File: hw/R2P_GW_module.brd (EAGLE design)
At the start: 40 x 40 mm, 32 parts, among them U1 STM32F103CX, U5 LD3985XX, X1 MICROMATCH-4

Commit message: First PCB version almost finished
Andrea Zoppi
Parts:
- removed U$1: ASE, crystal:ASE
- added C10, C13, C14, C15, C16, C17, C22, C23, C25, C26, C27, C8: 100n, rcl:C0603
- added C12: 4u7, rcl:C0805
- added C2, C3: 2u2, rcl:C0805
- added C24: 10u, rcl:C0805
- added C28: 15p, rcl:C0603
- added C4: 1u, rcl:C0805
- added OSC1: ASE 8MHz, crystal:ASE
- added OSC2: ASE 50MHz, crystal:ASE
- added R10, R15, R7: 2k2, rcl:R0603
- added R11, R14: 22, rcl:R0603
- added R12: 100k, rcl:R0603
- added R13: 1k5, rcl:R0603
- added R5: 47, rcl:R0603
- added R6: 4k87, rcl:R0603
- added R8, R9: 220, rcl:R0603
- added RN1, RN3, RN5: 51, resistor-dil:CAT16
- added RN2, RN4: 2k2, resistor-dil:CAT16
- added U2: DP83848C, texas-instruments:LQFP48
- added X2: 47589-0001, molex:47589-0001
- added X3: (no value), bel:SI-60062-F
- C11: value 15pF -> 15p
- C21: value 4.7u -> 4u7
- R2: value 10k -> 100k
- U1: value STM32F103CX -> STM32F407VG; device st:LQFP48 -> st:LQFP100
- moved C21 27.5 mm to (2.97, 25.5), turned to 90 degrees
- moved C20 24.2 mm to (8.54, 17.6), turned to 90 degrees
- moved C1 18.1 mm to (8.00, 38.0), turned to 90 degrees
- moved C11 16.7 mm to (28.0, 20.0), turned to 0 degrees
- moved R2 12.4 mm to (21.9, 15.5), turned to 270 degrees
- moved R3 10.0 mm to (28.0, 26.5), turned to 180 degrees
- moved U1 8.57 mm to (17.0, 26.0), turned to 180 degrees
- moved C19 6.40 mm to (24.1, 15.5)
- moved C18 1.19 mm to (28.0, 18.1), turned to 0 degrees
- moved X1 0.50 mm to (34.8, 35.2)
- renumbered SOT1 to U4, U5 to U3
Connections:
- removed net AM_DRDY: U1.41
- removed net AM_INT1: U1.42
- removed net AM_INT2: U1.43
- removed net BOOT0: R2.2, U1.44
- removed net GPS_RESET: U1.14
- removed net GPS_RX: U1.13
- removed net GPS_STATUS: U1.11
- removed net GPS_TX: U1.12
- removed net GYRO_CS: U1.18
- removed net GYRO_INT1: U1.21
- removed net GYRO_INT2: U1.19
- removed net MISO: U1.16
- removed net MOSI: U1.17
- removed net NRST: U$4.P$10, U1.7
- removed net OSC_IN: U$1.3, U1.5
- removed net OSC_OUT: U1.6
- removed net SCK: U1.15
- removed net SCL: U1.45
- removed net SDA: U1.46
- new net !ETH_PWRDN: OSC2.1, RN4.6, U2.7
- new net !RESET: R15.1, RN2.1, U$4.10, U1.14, U2.29
- new net ETH_RMII_CRS_DV: RN5.2, U1.32
- new net ETH_RMII_MDC: U1.16, U2.31
- new net ETH_RMII_MDIO: R13.1, U1.25, U2.30
- new net ETH_RMII_REF_CLK: OSC2.3, U1.24, U2.34
- new net ETH_RMII_RXD0: RN5.3, U1.33
- new net ETH_RMII_RXD1: RN5.4, U1.34
- new net ETH_RMII_TXD0: RN3.3, U1.51
- new net ETH_RMII_TXD1: RN3.4, U1.52
- new net ETH_RMII_TXEN: RN3.2, U1.48
- new net MCU_CLK: OSC1.3, U1.12
- new net N$10: RN1.3, U2.14, X3.4
- new net N$11: RN1.4, U2.13, X3.6
- new net N$12: R9.2, X3.YA
- new net N$13: C14.2, X3.2
- new net N$14: C17.1, C22.1, C23.1, C24.1, U2.18, U2.23, U2.37
- new net N$16: C16.2, X3.5
- new net N$17: R8.2, X3.GA
- new net N$19: RN2.3, U2.27
- new net N$21: RN3.7, U2.2
- new net N$23: RN2.2, U2.28, X3.YK
- new net N$24: RN2.4, U2.26, X3.GK
- new net N$25: RN3.6, U2.3
- new net N$26: R2.1, U1.94
- new net N$27: R7.1, U2.20
- new net N$28: R10.1, U2.21
- new net N$29: RN3.5, U2.4
- new net N$30: RN4.8, U2.5
- new net N$31: RN4.7, U2.6
- new net N$32: R14.2, X2.3
- new net N$34: RN5.6, U2.43
- new net N$38: R12.1, U2.39
- new net N$40: RN5.5, U2.44
- new net N$41: RN5.7, U2.40
- new net N$6: R6.1, U2.24
- new net N$7: R11.2, X2.2
- new net N$8: RN1.1, U2.17, X3.1
- new net N$9: RN1.2, U2.16, X3.3
- new net USB_DM: R11.1, U1.70
- new net USB_DP: R14.1, U1.71
- new net USB_ID: U1.69, X2.4
- new net USB_VBUS: U1.68, X2.1
- new net VCAP_1: C3.1, U1.49
- new net VCAP_2: C2.1, U1.73
- net +3V3: now also C10.1, C12.1, C13.1, C15.1, C25.1, C26.1, C27.1, C28.1, OSC1.4, OSC2.4, R10.2, R12.2, R13.2, R15.2, R5.2, R7.2, R8.1, R9.1, RN1.5, RN1.6, RN1.7, RN1.8, RN2.5, RN2.6, RN2.7, RN2.8, RN4.3, U$4.1, U1.100, U1.11, U1.19, U1.22, U1.28, U1.50, U1.6, U1.75, U2.22, U2.32, U2.48; no longer U$1.4, U$4.P$1, U1.1, U1.24, U1.36, U1.48, U1.9
- net CAN_RX: now also U1.81; no longer U1.32
- net CAN_TX: now also U1.82; no longer U1.33
- net GND: now also C10.2, C12.2, C13.2, C14.1, C15.2, C16.1, C17.2, C2.2, C22.2, C23.2, C24.2, C25.2, C26.2, C27.2, C28.2, C3.2, C4.2, C8.2, OSC1.2, OSC2.2, R2.2, R6.2, RN3.1, RN3.8, RN4.1, RN4.2, RN4.4, RN4.5, RN5.1, RN5.8, U$4.3, U$4.5, U$4.9, U1.10, U1.20, U1.27, U1.74, U1.99, U2.15, U2.19, U2.35, U2.36, U2.47, X2.5, X2.SHLD1, X2.SHLD2, X2.SHLD3, X2.SHLD4, X3.8, X3.SHLD1, X3.SHLD2; no longer R2.1, U$1.2, U$4.P$3, U$4.P$9, U1.23, U1.35, U1.47, U1.8
- net JTCK: now also U$4.4, U1.76; no longer U$4.P$4, U1.37
- net JTDI: now also U$4.8, U1.77; no longer U$4.P$8, U1.38
- net JTDO: now also U$4.6, U1.89; no longer U$4.P$6, U1.39
- net JTMS: now also U$4.2, U1.72; no longer U$4.P$2, U1.34
- net LED1: no longer U1.25
- net LED2: no longer U1.26
- net LED3: no longer U1.27
- net LED4: no longer U1.28
- net N$1: now also C4.1, C8.1, R5.1, U1.21; no longer U$4.P$5
- net N$3: now also OSC1.1; no longer U$1.1
- net UART_RX: now also U1.93; no longer U1.31
- net UART_TX: now also U1.92; no longer U1.30
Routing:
- net +3V3: track 116.2 -> 229.6 mm, vias 11 -> 12
- net !RESET: track 0.00 -> 48.8 mm, vias 0 -> 4
- net USB_ID: track 0.00 -> 46.3 mm, vias 0 -> 2
- net USB_VBUS: track 0.00 -> 44.8 mm, vias 0 -> 2
- net N$23: track 0.00 -> 36.4 mm, vias 0 -> 1
- net N$7: track 0.00 -> 34.8 mm, vias 0 -> 2
- net N$32: track 0.00 -> 33.7 mm, vias 0 -> 2
- net N$8: track 0.00 -> 33.5 mm
- net ETH_RMII_MDC: track 0.00 -> 31.9 mm, vias 0 -> 2
- net N$9: track 0.00 -> 29.4 mm
- net ETH_RMII_MDIO: track 0.00 -> 28.9 mm, vias 0 -> 3
- net N$14: track 0.00 -> 25.5 mm, vias 0 -> 2
- net N$24: track 0.00 -> 24.9 mm, vias 0 -> 1
- net N$10: track 0.00 -> 24.7 mm
- net ETH_RMII_REF_CLK: track 0.00 -> 24.7 mm
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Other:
- board size 40 x 40 mm -> 40 x 60 mm

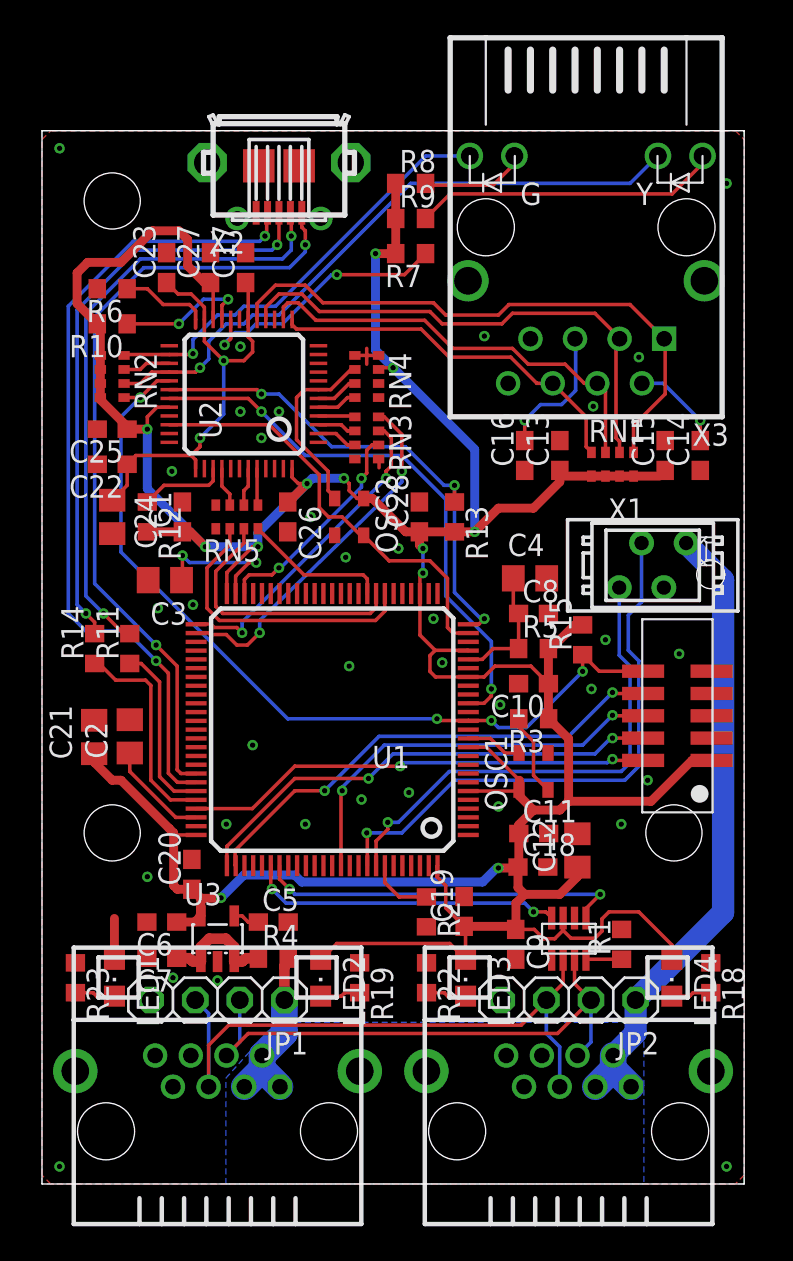
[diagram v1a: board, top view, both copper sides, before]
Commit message: All the PCB elements routed
The board has yet to be finally checked.

Andrea Zoppi
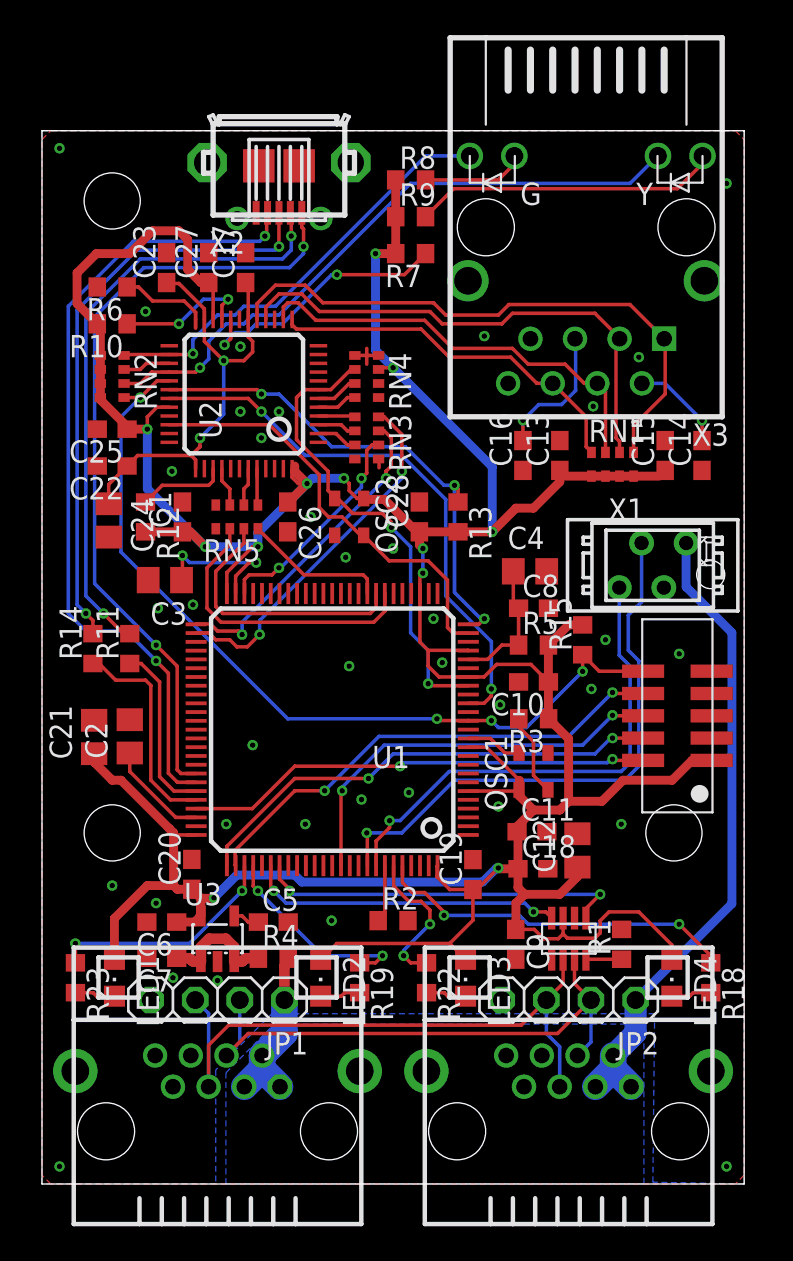
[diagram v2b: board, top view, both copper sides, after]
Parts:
- moved C19 2.16 mm to (24.6, 17.6)
- moved R2 1.96 mm to (20.0, 15.0), turned to 0 degrees
- moved C4 0.40 mm to (27.8, 34.9)
- moved C8 0.30 mm to (28.0, 32.8)
- moved C24 0.28 mm to (3.80, 37.8)
- moved R8 0.20 mm to (21.0, 57.2)
- moved R13 0.20 mm to (23.7, 38.0)
- moved R5 0.20 mm to (28.0, 30.7)
- moved C11 0.14 mm to (27.9, 20.1)
- moved C10 0.10 mm to (28.0, 28.6)
- moved C14 0.10 mm to (37.6, 41.5)
- moved C16 0.10 mm to (27.4, 41.5)
- moved C18 0.10 mm to (28.0, 18.0)
- moved C22 0.10 mm to (4.00, 40.9)
- moved R6 0.10 mm to (4.00, 51.1)
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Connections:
- net !ETH_PWRDN: now also U1.18
- net LED1: now also U1.78
- net LED2: now also U1.79
- net LED3: now also U1.95
- net LED4: now also U1.96
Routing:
- net LED4: track 0.00 -> 20.8 mm, vias 0 -> 2
- net !ETH_PWRDN: track 10.6 -> 26.8 mm, vias 0 -> 2
- net LED1: track 0.00 -> 13.3 mm, vias 0 -> 2
- net LED2: track 0.00 -> 11.6 mm, vias 0 -> 2
- net LED3: track 0.00 -> 8.62 mm, vias 0 -> 2
- net +3V3: track 229.6 -> 235.9 mm
- net GND: vias 35 -> 37

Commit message: Minor refinements
Andrea Zoppi
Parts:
- moved R5 5.20 mm to (27.9, 35.9)
- moved R3 4.72 mm to (30.5, 22.5), turned to 90 degrees
- moved C18 3.45 mm to (27.9, 21.4)
- moved C11 3.44 mm to (27.9, 23.5)
- moved OSC1 3.00 mm to (28.0, 26.5)
- moved C12 2.75 mm to (28.2, 17.5), turned to 0 degrees
- moved C4 1.10 mm to (27.9, 33.8)
- moved C8 1.10 mm to (28.0, 31.7)
- moved C10 1.00 mm to (28.0, 29.6), turned to 0 degrees
- moved R15 0.73 mm to (31.5, 30.8)
- moved C28 0.40 mm to (21.5, 38.4)
- moved R13 0.40 mm to (23.7, 38.4)
- moved C2 0.20 mm to (5.00, 25.3)
- moved C21 0.20 mm to (2.97, 25.3)
- moved C20 0.14 mm to (8.46, 17.8), turned to 270 degrees
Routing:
- net +3V3: track 235.9 -> 238.7 mm
- net N$3: track 4.74 -> 2.81 mm
- net MCU_CLK: track 3.24 -> 4.20 mm
- net !ETH_PWRDN: track 26.8 -> 26.2 mm
- net ETH_RMII_RXD1: track 8.25 -> 8.79 mm
- net GND: vias 37 -> 43

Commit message: Minor refinements
Andrea Zoppi
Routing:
- net CAN_TX: track 21.1 -> 20.0 mm
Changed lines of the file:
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@@
 <via x="10.5" y="20.5" extent="1-16" drill="0.3" shape="octagon"/>
 <via x="19.2" y="21.9" extent="1-16" drill="0.3" shape="octagon"/>
-<via x="11.3" y="44" extent="1-16" drill="0.3" shape="octagon"/>
+<via x="9" y="44" extent="1-16" drill="0.3" shape="octagon"/>
 <via x="31.3" y="28" extent="1-16" drill="0.3" shape="octagon"/>
-<via x="36.3" y="30.2" extent="1-16" drill="0.3" shape="octagon"/>
 <via x="26" y="19.1" extent="1-16" drill="0.3" shape="octagon"/>
 <via x="32.1" y="21.4" extent="1-16" drill="0.3" shape="octagon"/>
-<via x="20" y="36.3" extent="1-16" drill="0.3" shape="octagon"/>
-<via x="15.3" y="37.8" extent="1-16" drill="0.3" shape="octagon"/>
+<via x="20" y="36.4" extent="1-16" drill="0.3" shape="octagon"/>
+<via x="15.4" y="38" extent="1-16" drill="0.3" shape="octagon"/>
 <via x="17.3" y="35.7" extent="1-16" drill="0.3" shape="octagon"/>
 <via x="26.1" y="27.5" extent="1-16" drill="0.3" shape="octagon"/>
@@
 <via x="39" y="59" extent="1-16" drill="0.3" shape="octagon"/>
 <via x="1" y="59" extent="1-16" drill="0.3" shape="octagon"/>
-<via x="3.5" y="17" extent="1-16" drill="0.3" shape="octagon"/>
+<via x="1" y="30.5" extent="1-16" drill="0.3" shape="octagon"/>
 <via x="8.6" y="33" extent="1-16" drill="0.3" shape="octagon"/>
 <via x="6.6" y="32.8" extent="1-16" drill="0.3" shape="octagon"/>
@@
 <vertex x="9.9" y="6.5"/>
 </polygon>
-<via x="5.9" y="49.7" extent="1-16" drill="0.3" shape="octagon"/>
 <via x="29.9" y="26.8" extent="1-16" drill="0.3" shape="octagon"/>
 <via x="24.7" y="35" extent="1-16" drill="0.3" shape="octagon"/>
@@
 <via x="30.4" y="33.2" extent="1-16" drill="0.3" shape="octagon"/>
 <via x="29" y="20.1" extent="1-16" drill="0.3" shape="octagon"/>
+<via x="1" y="17" extent="1-16" drill="0.3" shape="octagon"/>
+<via x="38" y="17" extent="1-16" drill="0.3" shape="octagon"/>
 </signal>
 <signal name="+3V3">
@@
 <wire x1="3.325" y1="48.825" x2="3.325" y2="47.2" width="0.508" layer="1"/>
 <wire x1="20.15" y1="53" x2="20.15" y2="55.1" width="0.508" layer="1"/>
-<via x="6" y="43" extent="1-16" drill="0.3" shape="octagon"/>
-<wire x1="6" y1="43" x2="6" y2="43.7" width="0.2032" layer="1"/>
+<via x="6" y="43.5" extent="1-16" drill="0.3" shape="octagon"/>
+<wire x1="6" y1="43.5" x2="6" y2="43.7" width="0.2032" layer="1"/>
 <wire x1="6" y1="43.7" x2="6.55" y2="44.25" width="0.2032" layer="1"/>
 <wire x1="6.55" y1="44.25" x2="7.25" y2="44.25" width="0.2032" layer="1"/>
-<wire x1="4.85" y1="43" x2="6" y2="43" width="0.508" layer="1"/>
+<wire x1="4.85" y1="43" x2="5.5" y2="43" width="0.508" layer="1"/>
+<wire x1="5.5" y1="43" x2="6" y2="43.5" width="0.508" layer="1"/>
 <wire x1="20.15" y1="53" x2="19" y2="53" width="0.508" layer="1"/>
 <via x="19" y="53" extent="1-16" drill="0.3" shape="octagon"/>
@@
 <wire x1="8.45" y1="37.15" x2="8" y2="37.15" width="0.508" layer="1"/>
 <wire x1="5.9" y1="37.15" x2="8" y2="37.15" width="0.508" layer="1"/>
-<wire x1="6" y1="43" x2="6" y2="39.6" width="0.508" layer="16"/>
+<wire x1="6" y1="43.5" x2="6" y2="39.6" width="0.508" layer="16"/>
 <wire x1="9.2" y1="36.4" x2="6" y2="39.6" width="0.508" layer="16"/>
 <via x="17" y="40.2" extent="1-16" drill="0.3" shape="octagon"/>
@@
 <wire x1="38" y1="13.1" x2="36.3" y2="14.8" width="0.2032" layer="1"/>
 <via x="36.3" y="14.8" extent="1-16" drill="0.3" shape="octagon"/>
-<wire x1="36.3" y1="14.8" x2="27.7" y2="14.8" width="0.2032" layer="16"/>
-<wire x1="27.7" y1="14.8" x2="27.2" y2="15.3" width="0.2032" layer="16"/>
-<wire x1="27.2" y1="15.3" x2="22.9" y2="15.3" width="0.2032" layer="16"/>
+<wire x1="36.3" y1="14.8" x2="27.9" y2="14.8" width="0.2032" layer="16"/>
+<wire x1="27.9" y1="14.8" x2="27.4" y2="15.3" width="0.2032" layer="16"/>
+<wire x1="27.4" y1="15.3" x2="22.9" y2="15.3" width="0.2032" layer="16"/>
 <via x="22.9" y="15.3" extent="1-16" drill="0.3" shape="octagon"/>
 <wire x1="22.9" y1="15.3" x2="22.9" y2="15.5" width="0.2032" layer="1"/>
@@
 <via x="13.2" y="16.8" extent="1-16" drill="0.3" shape="octagon"/>
 <wire x1="13.2" y1="16.8" x2="14" y2="16" width="0.2032" layer="16"/>
-<wire x1="14" y1="16" x2="27.5" y2="16" width="0.2032" layer="16"/>
-<wire x1="27.5" y1="16" x2="28" y2="15.5" width="0.2032" layer="16"/>
-<via x="28" y="15.5" extent="1-16" drill="0.3" shape="octagon"/>
-<wire x1="28" y1="15.5" x2="28.7" y2="15.5" width="0.2032" layer="1"/>
+<wire x1="14" y1="16" x2="27.7" y2="16" width="0.2032" layer="16"/>
+<wire x1="27.7" y1="16" x2="28.2" y2="15.5" width="0.2032" layer="16"/>
+<via x="28.2" y="15.5" extent="1-16" drill="0.3" shape="octagon"/>
+<wire x1="28.2" y1="15.5" x2="28.7" y2="15.5" width="0.2032" layer="1"/>
 <wire x1="29.03625" y1="15.145" x2="29.03625" y2="15.16375" width="0.2032" layer="1"/>
 <wire x1="29.03625" y1="15.16375" x2="28.7" y2="15.5" width="0.2032" layer="1"/>
@@
 <via x="14.1" y="16.8" extent="1-16" drill="0.3" shape="octagon"/>
 <wire x1="14.1" y1="16.8" x2="14.4" y2="16.5" width="0.2032" layer="16"/>
-<wire x1="14.4" y1="16.5" x2="31.8" y2="16.5" width="0.2032" layer="16"/>
-<via x="31.8" y="16.5" extent="1-16" drill="0.3" shape="octagon"/>
+<wire x1="14.4" y1="16.5" x2="31" y2="16.5" width="0.2032" layer="16"/>
+<via x="31" y="16.5" extent="1-16" drill="0.3" shape="octagon"/>
 <wire x1="13.533159375" y1="18.131065625" x2="13.533159375" y2="17.366840625" width="0.2032" layer="1"/>
 <wire x1="13.533159375" y1="17.366840625" x2="14.1" y2="16.8" width="0.2032" layer="1"/>
-<wire x1="31.8" y1="16.5" x2="31" y2="15.7" width="0.2032" layer="1"/>
-<wire x1="31" y1="15.7" x2="31" y2="15.15875" width="0.2032" layer="1"/>
+<wire x1="31" y1="16.5" x2="31" y2="15.15875" width="0.2032" layer="1"/>
 <wire x1="31" y1="15.15875" x2="30.98625" y2="15.145" width="0.2032" layer="1"/>
 </signal>
@@
 <contactref element="R10" pad="1"/>
 <contactref element="U2" pad="21"/>
-<wire x1="4.85" y1="49" x2="7.8" y2="49" width="0.2032" layer="1"/>
-<via x="7.8" y="49" extent="1-16" drill="0.3" shape="octagon"/>
-<wire x1="7.8" y1="49" x2="9.2" y2="50.4" width="0.2032" layer="16"/>
-<wire x1="9.2" y1="50.4" x2="10.6" y2="50.4" width="0.2032" layer="16"/>
-<via x="10.6" y="50.4" extent="1-16" drill="0.3" shape="octagon"/>
-<wire x1="10.6" y1="50.4" x2="10.25" y2="50.05" width="0.2032" layer="1"/>
-<wire x1="10.25" y1="50.05" x2="10.25" y2="49.25" width="0.2032" layer="1"/>
+<wire x1="4.85" y1="49" x2="6.8" y2="49" width="0.2032" layer="1"/>
+<via x="6.8" y="49" extent="1-16" drill="0.3" shape="octagon"/>
+<wire x1="6.8" y1="49" x2="8.8" y2="49" width="0.2032" layer="16"/>
+<wire x1="8.8" y1="49" x2="10.2" y2="50.4" width="0.2032" layer="16"/>
+<wire x1="10.2" y1="50.4" x2="10.5" y2="50.4" width="0.2032" layer="16"/>
+<via x="10.5" y="50.4" extent="1-16" drill="0.3" shape="octagon"/>
+<wire x1="10.5" y1="50.4" x2="10.25" y2="50.15" width="0.2032" layer="1"/>
+<wire x1="10.25" y1="50.15" x2="10.25" y2="49.25" width="0.2032" layer="1"/>
 </signal>
 <signal name="!ETH_PWRDN">

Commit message: Minor refinements
Andrea Zoppi
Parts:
- C4: device rcl:C0805 -> rcl:C0603
- moved C15 18.1 mm to (21.0, 52.4), turned to 180 degrees
- moved RN1 14.3 mm to (21.0, 49.5), turned to 270 degrees
- moved C21 10.3 mm to (3.24, 15.0), turned to 180 degrees
- moved C13 9.66 mm to (21.0, 46.1), turned to 270 degrees
- moved C14 4.14 mm to (33.5, 42.1), turned to 0 degrees
- moved R7 1.50 mm to (21.0, 54.5), turned to 0 degrees
- moved R8 1.50 mm to (21.0, 58.7)
- moved R9 1.50 mm to (21.0, 56.6)
- moved C16 1.25 mm to (28.5, 42.1), turned to 0 degrees
- moved C20 0.20 mm to (8.26, 17.8)
- moved C4 0.10 mm to (28.0, 33.8)
- moved R5 0.10 mm to (28.0, 35.9)
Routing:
- net +3V3: track 238.9 -> 222.0 mm, vias 12 -> 9
- net N$8: track 33.5 -> 27.0 mm, vias 0 -> 1
- net N$9: track 29.3 -> 23.2 mm, vias 0 -> 1
- net N$11: track 21.4 -> 17.2 mm, vias 0 -> 1
- net N$10: track 24.6 -> 21.2 mm, vias 0 -> 1
- net N$13: track 5.45 -> 3.58 mm, vias 1 -> 0
- net N$16: track 7.82 -> 6.47 mm, vias 1 -> 0
- net N$27: track 15.3 -> 14.2 mm
- net N$12: track 17.5 -> 16.6 mm
- net N$17: track 5.89 -> 6.51 mm
- net ETH_RMII_RXD1: track 8.79 -> 8.26 mm
- net GND: vias 43 -> 42

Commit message: Minor refinements
Andrea Zoppi
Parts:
- renumbered 1 to X4, 2 to X5, U$4 to X6
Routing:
- net GND: vias 42 -> 44
